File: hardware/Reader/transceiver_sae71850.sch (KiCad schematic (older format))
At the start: 17 parts

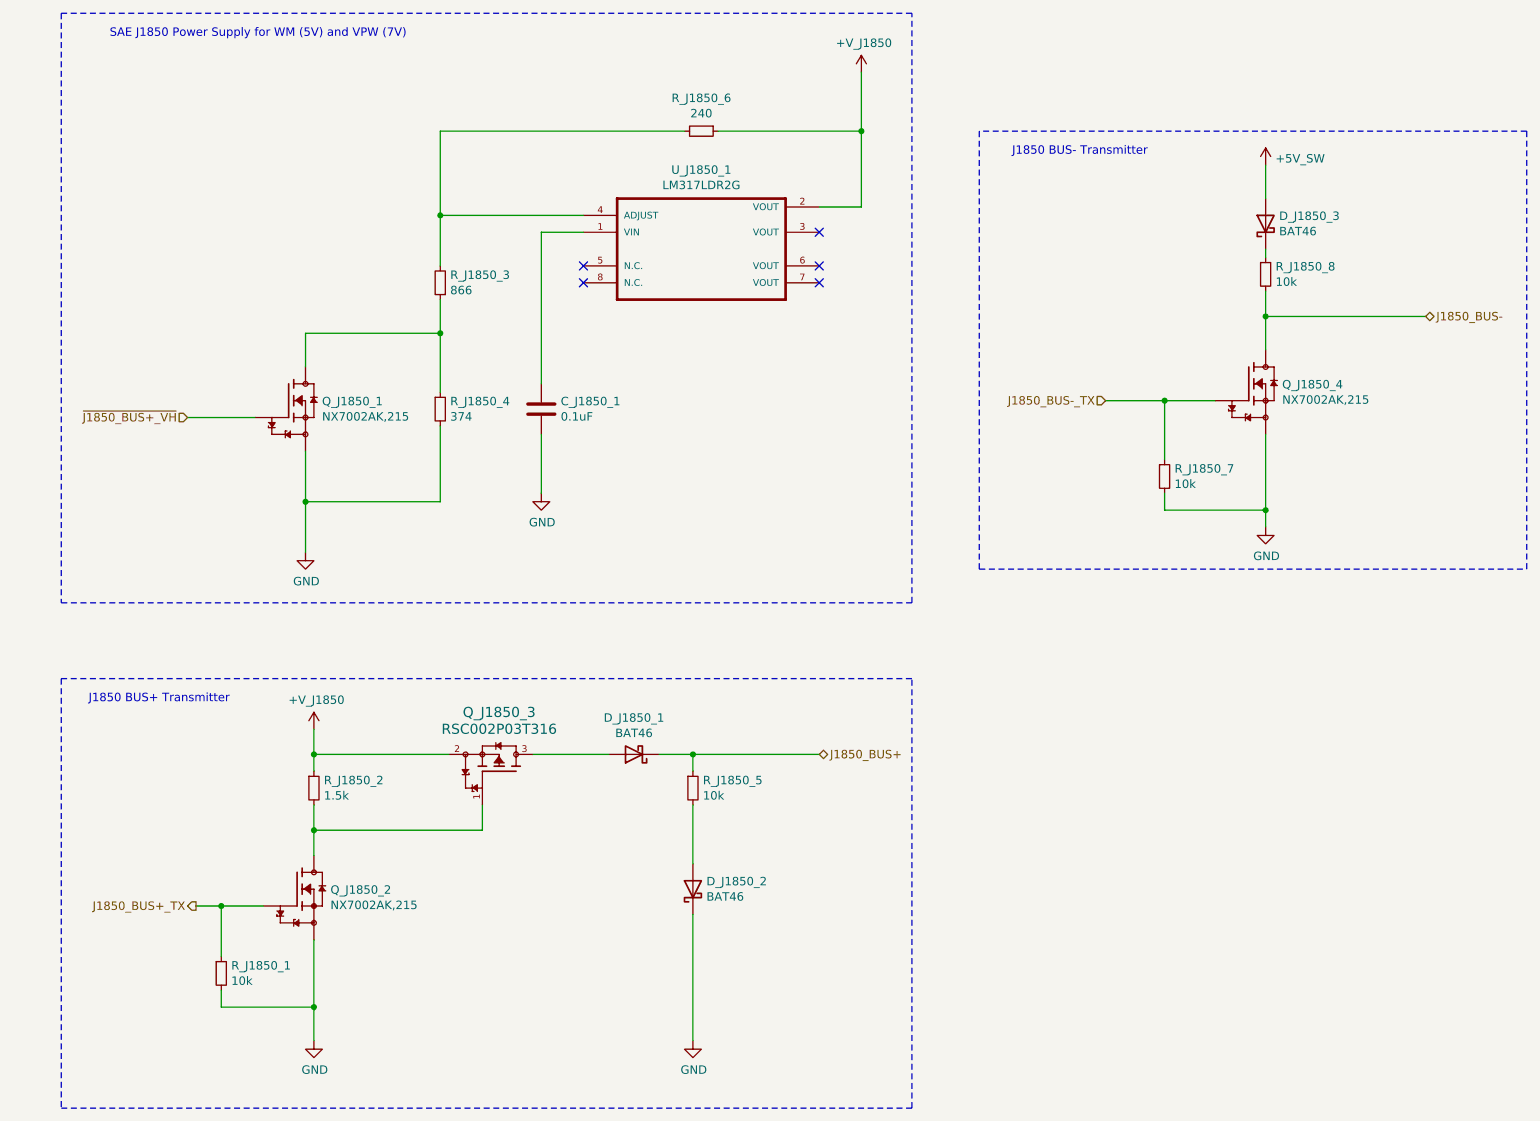
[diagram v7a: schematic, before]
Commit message: Fixed numerous bugs in design for Reader Schematic and PCB
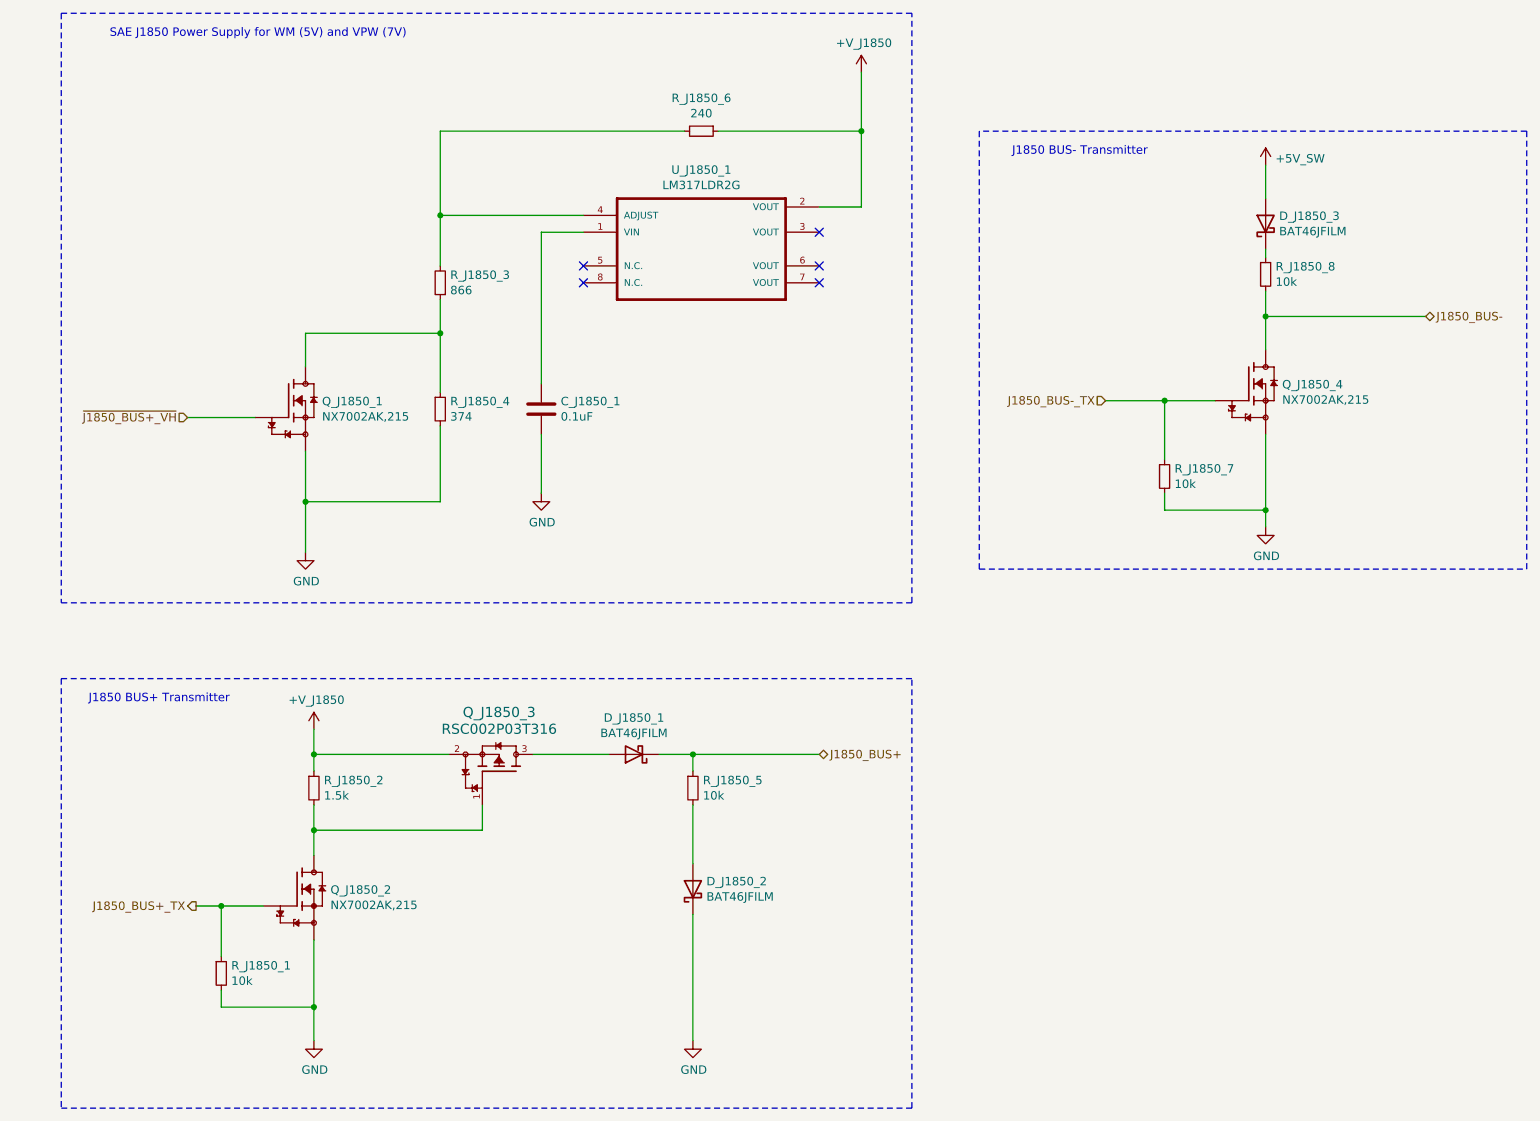
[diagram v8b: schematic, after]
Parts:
- D_J1850_1, D_J1850_2, D_J1850_3: value BAT46 -> BAT46JFILM; footprint Diode_THT:D_DO-35_SOD27_P7.62mm_Horizontal -> footprints:BAT46JFILM; Part Name BAT46 -> BAT46JFILM; digikeypn 497-3768-1-ND -> 497-6653-1-ND
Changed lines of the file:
@@
 P 4050 5100
 F 0 "D_J1850_1" H 4050 4883 50  0000 C CNN
-F 1 "BAT46" H 4050 4974 50  0000 C CNN
-F 2 "Diode_THT:D_DO-35_SOD27_P7.62mm_Horizontal" H 4050 4925 50  0001 C CNN
-F 3 "http://www.vishay.com/docs/85662/bat46.pdf" H 4050 5100 50  0001 C CNN
-F 4 "BAT46" H 4050 5100 50  0001 C CNN "Part Name"
+F 1 "BAT46JFILM" H 4050 4974 50  0000 C CNN
+F 2 "footprints:BAT46JFILM" H 4050 4925 50  0001 C CNN
+F 3 "https://www.st.com/content/ccc/resource/technical/document/datasheet/c6/32/d4/4a/28/d3/4b/11/CD00004930.pdf/files/CD00004930.pdf/jcr:content/translations/en.CD00004930.pdf" H 4050 5100 50  0001 C CNN
+F 4 "BAT46JFILM" H 4050 5100 50  0001 C CNN "Part Name"
 F 5 "STMicroelectronics" H 4050 5100 50  0001 C CNN "Manufacturer"
 F 6 "DigiKey Canada" H 4050 5100 50  0001 C CNN "Vendor"
-F 7 "497-3768-1-ND" H 4050 5100 50  0001 C CNN "digikeypn"
+F 7 "497-6653-1-ND" H 4050 5100 50  0001 C CNN "digikeypn"
 	1    4050 5100
 	-1   0    0    1
@@
 P 4400 5900
 F 0 "D_J1850_2" V 4446 5820 50  0000 R CNN
-F 1 "BAT46" V 4355 5820 50  0000 R CNN
-F 2 "Diode_THT:D_DO-35_SOD27_P7.62mm_Horizontal" H 4400 5725 50  0001 C CNN
-F 3 "http://www.vishay.com/docs/85662/bat46.pdf" H 4400 5900 50  0001 C CNN
-F 4 "BAT46" H 4400 5900 50  0001 C CNN "Part Name"
+F 1 "BAT46JFILM" V 4355 5820 50  0000 R CNN
+F 2 "footprints:BAT46JFILM" H 4400 5725 50  0001 C CNN
+F 3 "https://www.st.com/content/ccc/resource/technical/document/datasheet/c6/32/d4/4a/28/d3/4b/11/CD00004930.pdf/files/CD00004930.pdf/jcr:content/translations/en.CD00004930.pdf" H 4400 5900 50  0001 C CNN
+F 4 "BAT46JFILM" H 4400 5900 50  0001 C CNN "Part Name"
 F 5 "STMicroelectronics" H 4400 5900 50  0001 C CNN "Manufacturer"
 F 6 "DigiKey Canada" H 4400 5900 50  0001 C CNN "Vendor"
-F 7 "497-3768-1-ND" H 4400 5900 50  0001 C CNN "digikeypn"
+F 7 "497-6653-1-ND" H 4400 5900 50  0001 C CNN "digikeypn"
 	1    4400 5900
 	0    -1   -1   0
@@
 P 7800 1950
 F 0 "D_J1850_3" V 7846 1870 50  0000 R CNN
-F 1 "BAT46" V 7755 1870 50  0000 R CNN
-F 2 "Diode_THT:D_DO-35_SOD27_P7.62mm_Horizontal" H 7800 1775 50  0001 C CNN
-F 3 "http://www.vishay.com/docs/85662/bat46.pdf" H 7800 1950 50  0001 C CNN
-F 4 "BAT46" H 7800 1950 50  0001 C CNN "Part Name"
+F 1 "BAT46JFILM" V 7755 1870 50  0000 R CNN
+F 2 "footprints:BAT46JFILM" H 7800 1775 50  0001 C CNN
+F 3 "https://www.st.com/content/ccc/resource/technical/document/datasheet/c6/32/d4/4a/28/d3/4b/11/CD00004930.pdf/files/CD00004930.pdf/jcr:content/translations/en.CD00004930.pdf" H 7800 1950 50  0001 C CNN
+F 4 "BAT46JFILM" H 7800 1950 50  0001 C CNN "Part Name"
 F 5 "STMicroelectronics" H 7800 1950 50  0001 C CNN "Manufacturer"
 F 6 "DigiKey Canada" H 7800 1950 50  0001 C CNN "Vendor"
-F 7 "497-3768-1-ND" H 7800 1950 50  0001 C CNN "digikeypn"
+F 7 "497-6653-1-ND" H 7800 1950 50  0001 C CNN "digikeypn"
 	1    7800 1950
 	0    -1   -1   0
